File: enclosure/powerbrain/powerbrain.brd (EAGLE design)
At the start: 24.8 x 64.8 mm, 42 parts, among them Q2 200mA/50V, X2 ZX62D-B-5PA8

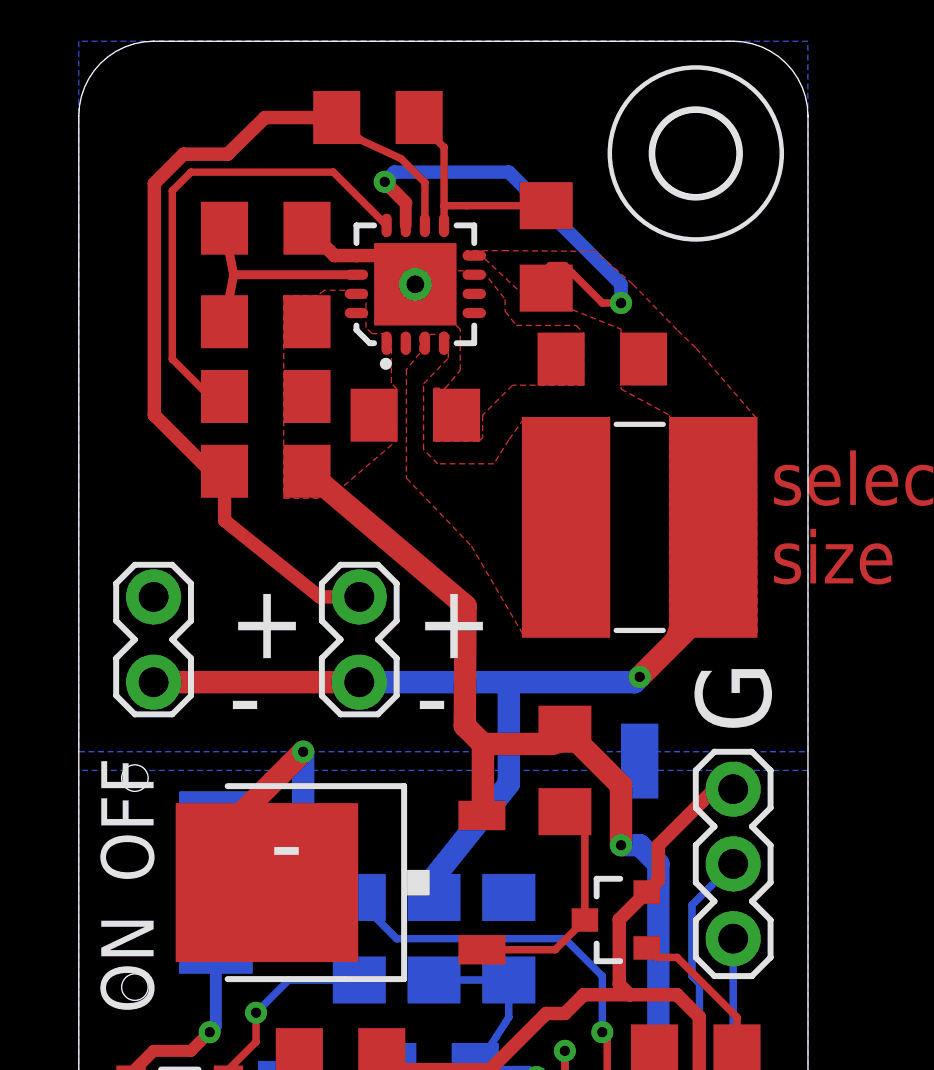
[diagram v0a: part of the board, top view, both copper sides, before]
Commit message: powerbrain: resistor/capacitor values for boost converter
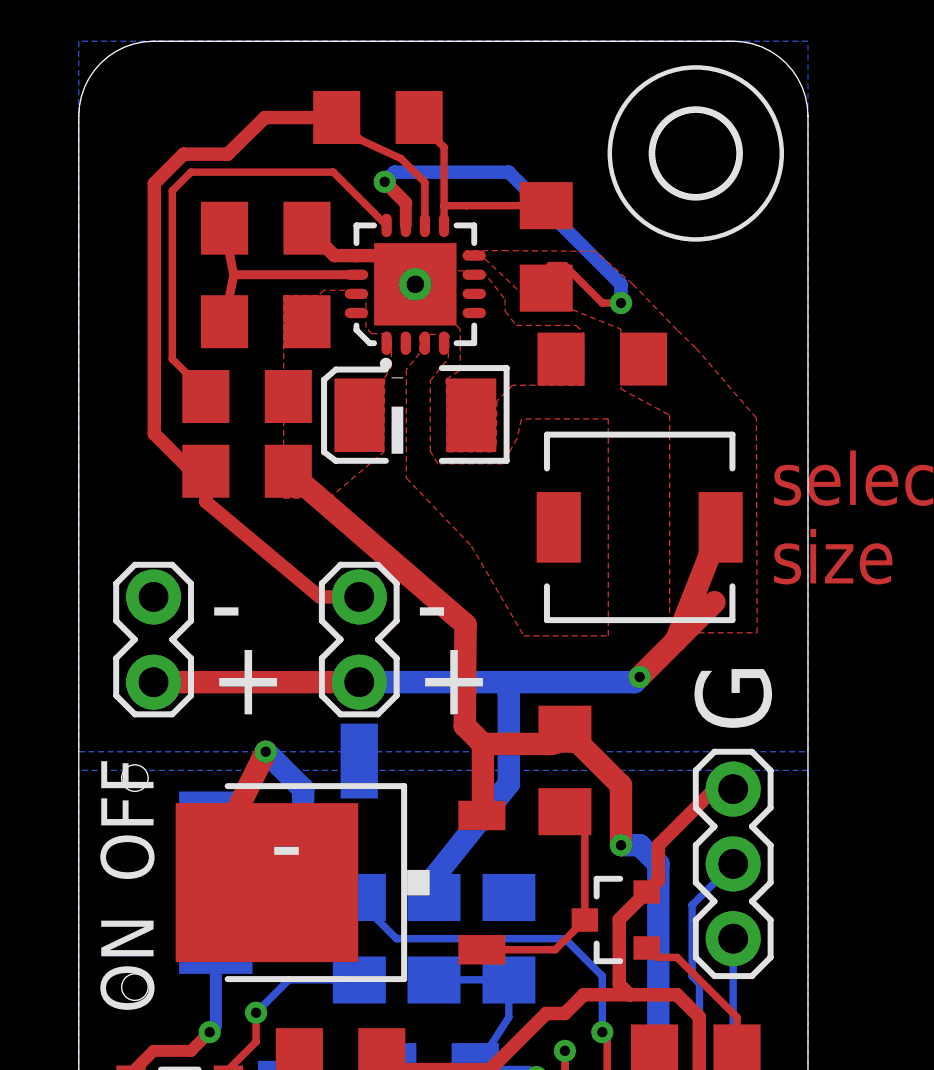
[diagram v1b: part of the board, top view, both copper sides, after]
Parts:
- removed BC3: (no value), SparkFun-Capacitors:1206
- added C7: 100uF / 6V, SparkFun-Passives:EIA3528-KIT
- BC1: value (none) -> 10uF
- BC2: value (none) -> 2.2uF
- BL1: device SparkFun-Passives:NPI75C -> SparkFun-Passives:B82462G
- BR1, BR3: value (none) -> 1.87M
- BR2: value (none) -> 340k
- BR4: value (none) -> 200k
- moved SH2 9.53 mm to (9.53, 40.3)
- moved BC2 0.63 mm to (5.71, 50.2)
- moved BR5 0.63 mm to (5.71, 52.7)
- turned BL1 to 90 degrees
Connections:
- net BATT_GND: now also C7.C; no longer BC3.1
- net BATT_VCC: now also BL1.P$2; no longer BL1.2
- net B_SW: now also BL1.P$1; no longer BL1.1
- net VCC: now also C7.A; no longer BC3.2
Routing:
- net BATT_GND: track 35.7 -> 35.0 mm

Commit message: powerbrain: small improvements
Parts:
- removed S2: (no value), SparkFun-Electromechanical:SWITCH-SPDT-SMD
- added TP1, TP2: TPSQTP20R, testpad:TP20R
- moved BR2 3.86 mm to (14.0, 62.8)
- moved BC2 1.27 mm to (5.71, 51.4)
- moved BL1 1.27 mm to (19.1, 49.5)
- moved BR1 1.27 mm to (15.9, 59.1)
- moved BR3 1.27 mm to (6.35, 56.5)
- moved BR5 1.27 mm to (5.71, 54.0)
- moved C7 1.27 mm to (11.4, 53.3)
- moved BC1 1.27 mm to (17.8, 55.2)
- moved BR4 1.27 mm to (6.35, 59.7)
- moved U2 1.27 mm to (11.4, 57.8)
- moved J1 0.90 mm to (10.2, 46.4)
- moved J4 0.63 mm to (2.54, 46.4)
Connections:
- removed net USB_VCC_OUT: F2.1, S2.3, X2.1
- net GND: now also TP2.TP
- net USB_VCC: now also F2.1, TP1.TP, X2.1; no longer S2.2
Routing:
- net USB_VCC_OUT: track 17.2 -> 0.00 mm, vias 1 -> 0
- net USB_VCC: track 12.3 -> 22.9 mm
- net BATT_VCC: track 48.4 -> 44.6 mm
- net BATT_GND: track 35.0 -> 37.7 mm
- net VCC: track 95.1 -> 97.7 mm
- net B_LBI: track 7.84 -> 7.30 mm
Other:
- board text added: "5V"
- board text added: "GND"
- board text removed: "OFF"
- board text removed: "ON"
